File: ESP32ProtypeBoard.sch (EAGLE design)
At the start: 92 parts, among them IC1 ACT4088US-T, IC2 SI4431BDY, J10 POWER_JACKPTH_LOCK, Q2 MMBT3904, Q3 MMBT3904, Q4 BSS138, U2 ESP-WROOM-32

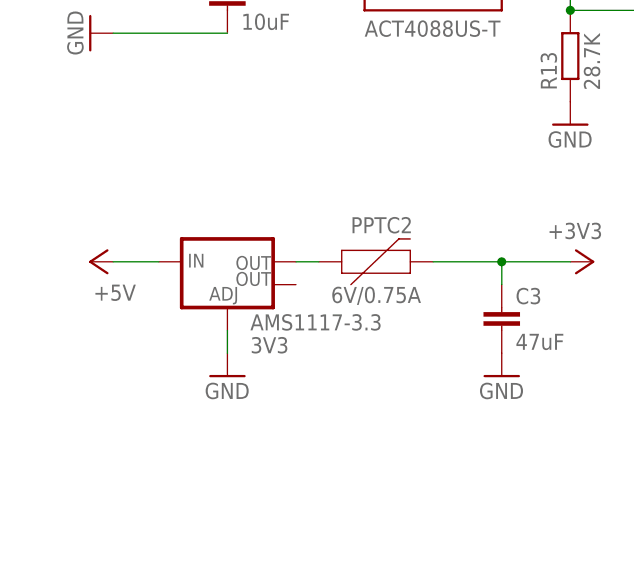
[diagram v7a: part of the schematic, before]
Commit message: Placed power curcuit for now
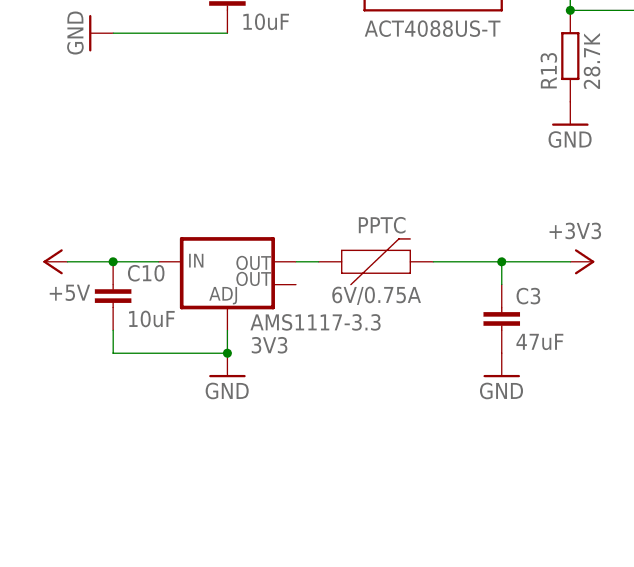
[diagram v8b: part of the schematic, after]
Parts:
- added C10: 10uF, rcl:C-EUC0805K
- RESET: value SWITCH_MOMENTARY_2PIN -> MOMENTARY-SWITCH-SPST-SMD-4.5MM; device SPST_2PIN_DPS_SWITCH:SWITCH_MOMENTARY_2PIN -> SparkFun-Switches:MOMENTARY-SWITCH-SPST-SMD-4.5MM
- renumbered PPTC2 to PPTC
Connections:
- net N$13 renamed SW
- net N$14 renamed BST
- net N$17 renamed FB
- net +5V: now also C10.1
- net GND: now also C10.2
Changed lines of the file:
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@@
 <part name="GND6" library="supply1" library_urn="urn:adsk.eagle:library:371" deviceset="GND" device=""/>
 <part name="GND8" library="supply1" library_urn="urn:adsk.eagle:library:371" deviceset="GND" device=""/>
-<part name="RESET" library="SPST_2PIN_DPS_SWITCH" deviceset="SWITCH_MOMENTARY_2PIN" device="" value="SWITCH_MOMENTARY_2PIN"/>
+<part name="RESET" library="SparkFun-Switches" library_urn="urn:adsk.eagle:library:535" deviceset="MOMENTARY-SWITCH-SPST" device="-SMD-4.5MM" package3d_urn="urn:adsk.eagle:package:40162/1" value="MOMENTARY-SWITCH-SPST-SMD-4.5MM"/>
 <part name="GND19" library="supply1" library_urn="urn:adsk.eagle:library:371" deviceset="GND" device=""/>
 <part name="+3V3" library="supply1" library_urn="urn:adsk.eagle:library:371" deviceset="+3V3" device=""/>
@@
 <part name="+3V2" library="supply1" library_urn="urn:adsk.eagle:library:371" deviceset="+3V3" device=""/>
 <part name="P+11" library="supply1" library_urn="urn:adsk.eagle:library:371" deviceset="VCC" device=""/>
-<part name="PPTC2" library="SparkFun-Fuses" library_urn="urn:adsk.eagle:library:517" deviceset="PPTC" device="_THREE-QUARTER-AMP" package3d_urn="urn:adsk.eagle:package:38575/1" value="6V/0.75A"/>
+<part name="PPTC" library="SparkFun-Fuses" library_urn="urn:adsk.eagle:library:517" deviceset="PPTC" device="_THREE-QUARTER-AMP" package3d_urn="urn:adsk.eagle:package:38575/1" value="6V/0.75A"/>
 <part name="+3V10" library="supply1" library_urn="urn:adsk.eagle:library:371" deviceset="+3V3" device=""/>
 <part name="GND4" library="supply1" library_urn="urn:adsk.eagle:library:371" deviceset="GND" device=""/>
@@
 <part name="R13" library="rcl" library_urn="urn:adsk.eagle:library:334" deviceset="R-EU_" device="R0805" package3d_urn="urn:adsk.eagle:package:23553/2" value="28.7K"/>
 <part name="GND22" library="supply1" library_urn="urn:adsk.eagle:library:371" deviceset="GND" device=""/>
+<part name="C10" library="rcl" library_urn="urn:adsk.eagle:library:334" deviceset="C-EU" device="C0805K" package3d_urn="urn:adsk.eagle:package:23681/2" value="10uF"/>
 </parts>
 <sheets>
@@
 <attribute name="VALUE" x="170.18" y="43.18" size="1.778" layer="96" rot="R270"/>
 </instance>
-<instance part="RESET" gate="&gt;NAME" x="274.32" y="60.96" smashed="yes" rot="MR0">
+<instance part="RESET" gate="G$1" x="274.32" y="60.96" smashed="yes" rot="MR0">
 <attribute name="NAME" x="274.32" y="62.484" size="1.778" layer="95" font="vector" rot="MR0" align="bottom-center"/>
 </instance>
@@
 <attribute name="VALUE" x="101.6" y="66.04" size="1.778" layer="96"/>
 </instance>
-<instance part="P+5" gate="1" x="-2.54" y="25.4" smashed="yes" rot="R90">
-<attribute name="VALUE" x="2.54" y="22.86" size="1.778" layer="96" rot="R180"/>
+<instance part="P+5" gate="1" x="-7.62" y="25.4" smashed="yes" rot="R90">
+<attribute name="VALUE" x="-2.54" y="22.86" size="1.778" layer="96" rot="R180"/>
 </instance>
 <instance part="C8" gate="G$1" x="10.16" y="93.98" smashed="yes">
@@
 <attribute name="VALUE" x="38.1" y="93.98" size="1.778" layer="96" rot="R180"/>
 </instance>
-<instance part="PPTC2" gate="G$1" x="27.94" y="25.4" smashed="yes">
+<instance part="PPTC" gate="G$1" x="27.94" y="25.4" smashed="yes">
 <attribute name="NAME" x="29.845" y="28.575" size="1.778" layer="95" font="vector" align="bottom-center"/>
 <attribute name="VALUE" x="29.21" y="22.606" size="1.778" layer="96" font="vector" align="top-center"/>
@@
 <instance part="GND22" gate="1" x="50.8" y="40.64" smashed="yes">
 <attribute name="VALUE" x="48.26" y="38.1" size="1.778" layer="96"/>
+</instance>
+<instance part="C10" gate="G$1" x="0" y="22.86" smashed="yes">
+<attribute name="NAME" x="1.524" y="23.241" size="1.778" layer="95"/>
+<attribute name="VALUE" x="1.524" y="18.161" size="1.778" layer="96"/>
 </instance>
 </instances>
@@
 <pinref part="GND11" gate="1" pin="GND"/>
 <wire x1="12.7" y1="15.24" x2="12.7" y2="17.78" width="0.1524" layer="91"/>
+<pinref part="C10" gate="G$1" pin="2"/>
+<wire x1="12.7" y1="15.24" x2="0" y2="15.24" width="0.1524" layer="91"/>
+<wire x1="0" y1="15.24" x2="0" y2="17.78" width="0.1524" layer="91"/>
+<junction x="12.7" y="15.24"/>
 </segment>
 <segment>
@@
 <pinref part="GND19" gate="1" pin="GND"/>
 <wire x1="266.7" y1="68.58" x2="266.7" y2="60.96" width="0.1524" layer="91"/>
-<pinref part="RESET" gate="&gt;NAME" pin="2"/>
+<pinref part="RESET" gate="G$1" pin="2"/>
 <wire x1="269.24" y1="60.96" x2="266.7" y2="60.96" width="0.1524" layer="91"/>
 <junction x="266.7" y="60.96"/>
@@
 <pinref part="+3V4" gate="G$1" pin="+3V3"/>
 <wire x1="43.18" y1="25.4" x2="50.8" y2="25.4" width="0.1524" layer="91"/>
-<pinref part="PPTC2" gate="G$1" pin="2"/>
+<pinref part="PPTC" gate="G$1" pin="2"/>
 <wire x1="35.56" y1="25.4" x2="43.18" y2="25.4" width="0.1524" layer="91"/>
 <pinref part="C3" gate="G$1" pin="1"/>
@@
 <wire x1="276.86" y1="68.58" x2="281.94" y2="68.58" width="0.1524" layer="91"/>
 <junction x="281.94" y="68.58"/>
-<pinref part="RESET" gate="&gt;NAME" pin="1"/>
+<pinref part="RESET" gate="G$1" pin="1"/>
 <wire x1="279.4" y1="60.96" x2="281.94" y2="60.96" width="0.1524" layer="91"/>
 <junction x="281.94" y="60.96"/>
@@
 <segment>
 <pinref part="AMS1117-3.3" gate="G$1" pin="IN"/>
+<wire x1="-5.08" y1="25.4" x2="0" y2="25.4" width="0.1524" layer="91"/>
+<pinref part="P+5" gate="1" pin="+5V"/>
+<pinref part="C10" gate="G$1" pin="1"/>
 <wire x1="0" y1="25.4" x2="5.08" y2="25.4" width="0.1524" layer="91"/>
-<pinref part="P+5" gate="1" pin="+5V"/>
+<junction x="0" y="25.4"/>
 </segment>
 <segment>
@@
 <pinref part="AMS1117-3.3" gate="G$1" pin="OUT"/>
 <wire x1="20.32" y1="25.4" x2="22.86" y2="25.4" width="0.1524" layer="91"/>
-<pinref part="PPTC2" gate="G$1" pin="1"/>
+<pinref part="PPTC" gate="G$1" pin="1"/>
 </segment>
 </net>
@@
 </segment>
 </net>
-<net name="N$13" class="0">
+<net name="SW" class="0">
 <segment>
 <pinref part="IC1" gate="G$1" pin="SW"/>
@@
 </segment>
 </net>
-<net name="N$14" class="0">
+<net name="BST" class="0">
 <segment>
 <pinref part="C7" gate="G$1" pin="2"/>
@@
 </segment>
 </net>
-<net name="N$17" class="0">
+<net name="FB" class="0">
 <segment>
 <pinref part="IC1" gate="G$1" pin="FB"/>
